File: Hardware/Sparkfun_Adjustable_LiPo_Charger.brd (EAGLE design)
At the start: 31.8 x 31.8 mm, 26 parts, among them SW1 DIP-06, U1 MCP73831

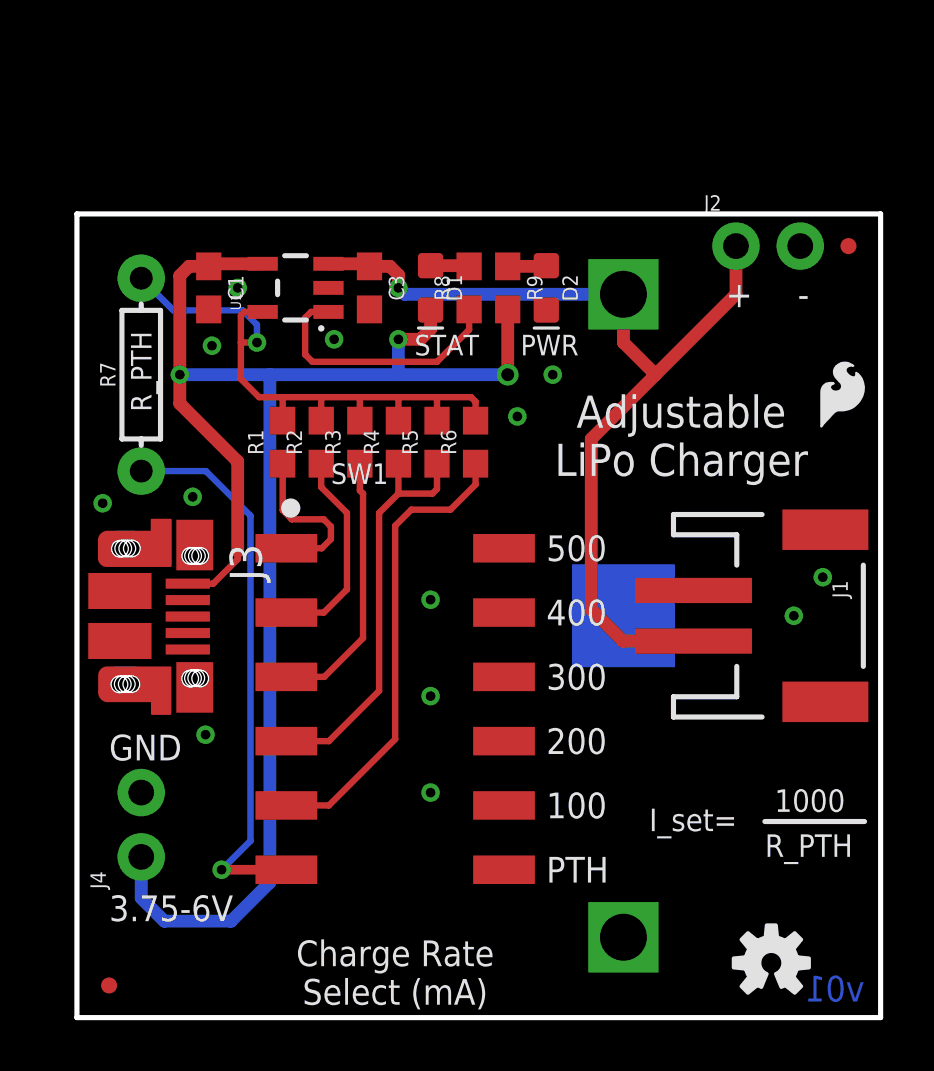
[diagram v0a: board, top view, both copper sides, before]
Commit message: Design Review Changes
Replaced PTH coin cell holder with SMD
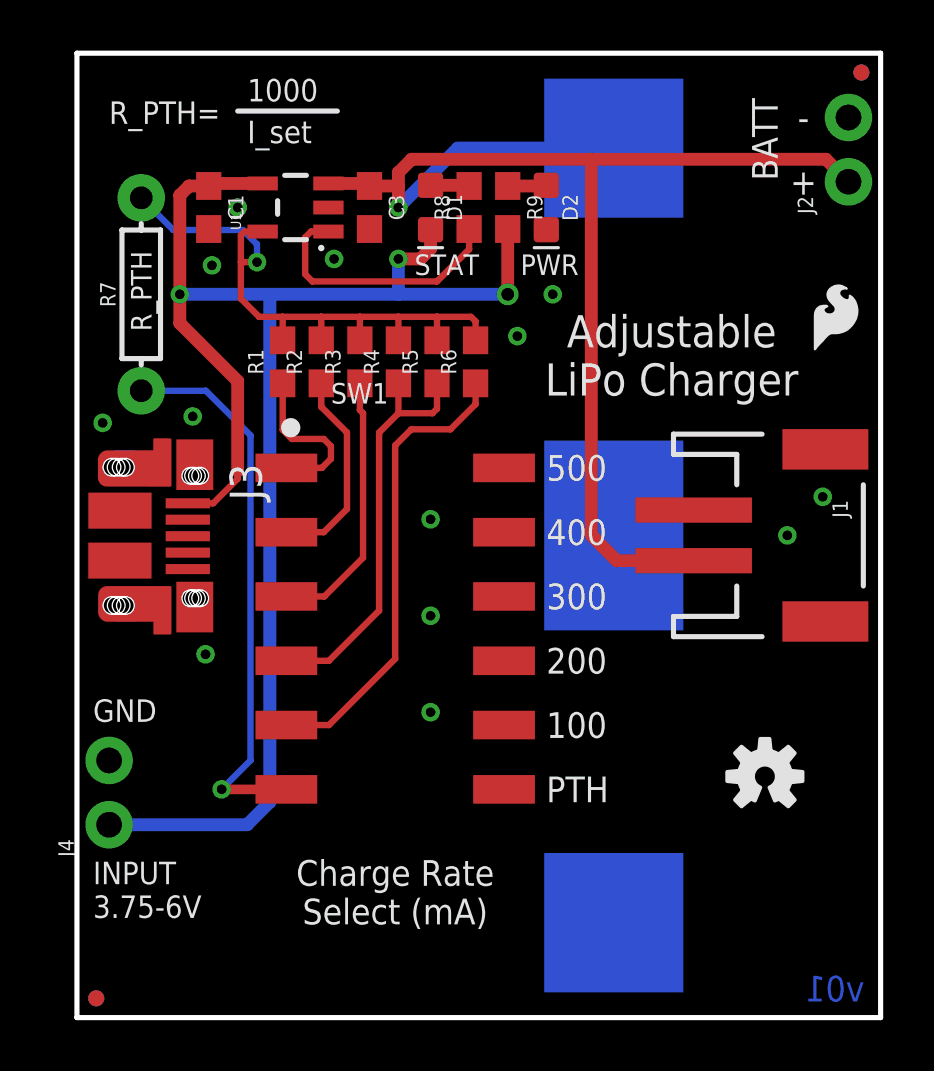
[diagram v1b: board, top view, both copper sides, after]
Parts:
- added FD3, FD4: FIDUCIALUFIDUCIAL, SparkFun-Aesthetics:FIDUCIAL-MICRO
- BT1: device SparkFun-Batteries:BATTCON_24.5MM_PTH -> SparkFun-Batteries:BATTCON_24.5MM_SMD
- moved LOGO2 7.37 mm to (27.2, 9.53)
- moved FD1 6.88 mm to (31.0, 37.3)
- moved J2 5.12 mm to (30.5, 33.0), turned to 90 degrees
- moved U$1 3.29 mm to (15.6, 1.91)
- moved BT1 3.20 mm to (21.2, 19.1)
- moved J1 3.18 mm to (28.1, 19.1)
- moved J3 3.18 mm to (3.05, 19.1)
- moved R1 3.18 mm to (8.13, 25.9)
- moved R2 3.18 mm to (9.65, 25.9)
- moved R3 3.18 mm to (11.2, 25.9)
- moved R4 3.18 mm to (12.7, 25.9)
- moved R5 3.18 mm to (14.2, 25.9)
- moved R6 3.18 mm to (15.7, 25.9)
- moved R7 3.18 mm to (2.54, 28.6)
- moved SW1 3.18 mm to (12.6, 15.4)
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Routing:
- net V_BATT: track 37.5 -> 51.4 mm
- net VCC: track 64.9 -> 63.9 mm
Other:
- board size 31.8 x 31.8 mm -> 31.8 x 38.1 mm
- board text added: "BATT"
- board text added: "INPUT 3.75-6V"
- board text added: "I_set"
- board text added: "R_PTH="
- board text removed: "3.75-6V"
- board text removed: "I_set="

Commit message: Proto Changes
Fixed layout error of D1 to the correct orientation
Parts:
- turned D1 to 90 degrees
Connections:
- net N$8: now also D1.C; no longer D1.A
- net VCC: now also D1.A; no longer D1.C
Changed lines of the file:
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@@
 <setting verticaltext="up"/>
 </settings>
-<grid distance="0.1" unitdist="inch" unit="inch" style="lines" multiple="1" display="yes" altdistance="0.005" altunitdist="inch" altunit="inch"/>
+<grid distance="0.05" unitdist="inch" unit="inch" style="lines" multiple="1" display="yes" altdistance="0.005" altunitdist="inch" altunit="inch"/>
 <layers>
 <layer number="1" name="Top" color="4" fill="1" visible="yes" active="yes"/>
@@
 <layer number="20" name="Dimension" color="15" fill="1" visible="yes" active="yes"/>
 <layer number="21" name="tPlace" color="16" fill="1" visible="yes" active="yes"/>
-<layer number="22" name="bPlace" color="14" fill="1" visible="no" active="yes"/>
+<layer number="22" name="bPlace" color="14" fill="1" visible="yes" active="yes"/>
 <layer number="23" name="tOrigins" color="15" fill="1" visible="yes" active="yes"/>
-<layer number="24" name="bOrigins" color="15" fill="1" visible="no" active="yes"/>
+<layer number="24" name="bOrigins" color="15" fill="1" visible="yes" active="yes"/>
 <layer number="25" name="tNames" color="7" fill="1" visible="no" active="yes"/>
 <layer number="26" name="bNames" color="7" fill="1" visible="no" active="yes"/>
@@
 <layer number="43" name="vRestrict" color="2" fill="10" visible="no" active="yes"/>
 <layer number="44" name="Drills" color="7" fill="1" visible="no" active="yes"/>
-<layer number="45" name="Holes" color="7" fill="1" visible="no" active="yes"/>
+<layer number="45" name="Holes" color="7" fill="1" visible="yes" active="yes"/>
 <layer number="46" name="Milling" color="3" fill="1" visible="no" active="yes"/>
 <layer number="47" name="Measures" color="7" fill="1" visible="no" active="yes"/>
@@
 <text x="6.731" y="36.195" size="0.889" layer="21" font="vector" ratio="15">1000</text>
 <wire x1="6.35" y1="35.814" x2="10.287" y2="35.814" width="0.2032" layer="21"/>
-<text x="28.702" y="33.02" size="1.016" layer="21" font="vector" ratio="15" align="center">+</text>
-<text x="28.702" y="35.56" size="1.016" layer="21" font="vector" ratio="15" align="center">-</text>
+<text x="28.829" y="33.02" size="1.016" layer="21" font="vector" ratio="15" rot="R180" align="center">+</text>
+<text x="28.702" y="35.56" size="1.016" layer="21" font="vector" ratio="15" rot="R90" align="center">-</text>
 <text x="23.495" y="26.162" size="1.27" layer="21" font="vector" ratio="15" align="center">Adjustable
 LiPo Charger</text>
 <text x="2.54" y="28.702" size="0.8128" layer="21" font="vector" ratio="15" rot="R90" align="center">R_PTH</text>
 <text x="28.702" y="33.02" size="1.016" layer="22" font="vector" ratio="15" rot="MR0" align="center">+</text>
-<text x="28.702" y="35.56" size="1.016" layer="22" font="vector" ratio="15" rot="MR0" align="center">-</text>
+<text x="28.702" y="35.56" size="1.016" layer="22" font="vector" ratio="15" rot="MR270" align="center">-</text>
 <text x="0.635" y="3.937" size="0.889" layer="21" font="vector" ratio="15">INPUT
 3.75-6V</text>
@@
 <attribute name="PROD_ID" value="CAP-08280" x="11.557" y="32.004" size="1.778" layer="27" rot="R270" display="off"/>
 </element>
-<element name="D1" library="SparkFun-LED" package="LED-0603" value="BLUE" x="13.97" y="32.004" rot="R270">
-<attribute name="PROD_ID" value="DIO-08575" x="13.97" y="32.004" size="1.778" layer="27" rot="R270" display="off"/>
+<element name="D1" library="SparkFun-LED" package="LED-0603" value="BLUE" x="13.97" y="32.004" rot="SR90">
+<attribute name="PROD_ID" value="DIO-08575" x="13.97" y="32.004" size="1.778" layer="27" rot="SR90" display="off"/>
 </element>
 <element name="FD1" library="SparkFun-Aesthetics" package="FIDUCIAL-MICRO" value="FIDUCIALUFIDUCIAL" x="30.988" y="37.338"/>
@@
 <wire x1="6.858" y1="10.16" x2="5.715" y2="9.017" width="0.254" layer="16"/>
 </signal>
-<signal name="N$8">
-<contactref element="R8" pad="2"/>
-<contactref element="D1" pad="A"/>
-<wire x1="13.97" y1="32.881" x2="15.494" y2="32.881" width="0.508" layer="1"/>
-<wire x1="15.494" y1="32.881" x2="15.494" y2="32.854" width="0.508" layer="1"/>
-</signal>
 <signal name="PROG">
 <contactref element="U1" pad="5"/>
@@
 <contactref element="U1" pad="4"/>
 <contactref element="C1" pad="1"/>
-<contactref element="D1" pad="C"/>
 <via x="12.7" y="29.972" extent="1-16" drill="0.381"/>
 <wire x1="6.35" y1="21.59" x2="6.35" y2="25.146" width="0.508" layer="1"/>
@@
 <wire x1="12.7" y1="29.972" x2="13.56839375" y2="29.972" width="0.508" layer="1"/>
 <wire x1="13.56839375" y1="29.972" x2="13.97" y2="30.37360625" width="0.508" layer="1"/>
-<wire x1="13.97" y1="30.37360625" x2="13.97" y2="31.127" width="0.508" layer="1"/>
 <wire x1="7.3359" y1="32.954" x2="5.207" y2="32.954" width="0.508" layer="1"/>
 <wire x1="5.207" y1="32.954" x2="5.207" y2="32.854" width="0.508" layer="1"/>
@@
 <wire x1="6.72571875" y1="7.62" x2="1.27" y2="7.62" width="0.508" layer="16"/>
 <wire x1="7.62" y1="8.51428125" x2="6.72571875" y2="7.62" width="0.508" layer="16"/>
+<contactref element="D1" pad="A"/>
+<wire x1="13.97" y1="30.37360625" x2="13.97" y2="31.127" width="0.508" layer="1"/>
 </signal>
 <signal name="N$1">
@@
 <wire x1="18.542" y1="32.854" x2="18.542" y2="32.881" width="0.508" layer="1"/>
 </signal>
+<signal name="N$8">
+<contactref element="R8" pad="2"/>
+<contactref element="D1" pad="C"/>
+<wire x1="13.97" y1="32.881" x2="15.467" y2="32.881" width="0.254" layer="1"/>
+<wire x1="15.467" y1="32.881" x2="15.494" y2="32.854" width="0.254" layer="1"/>
+</signal>
 </signals>

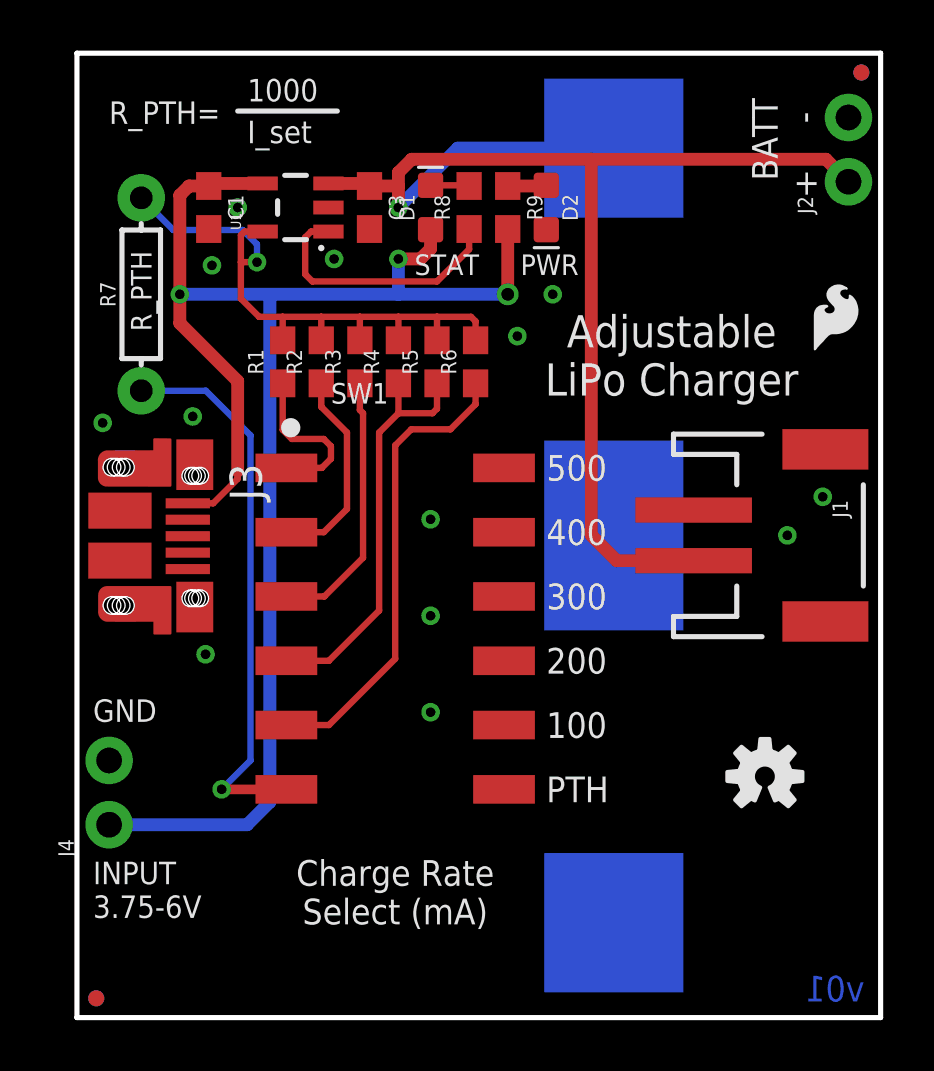
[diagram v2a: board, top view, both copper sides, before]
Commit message: v10 changes
- Added switch label to indicate on/off position.
- Added units to charge rate equation
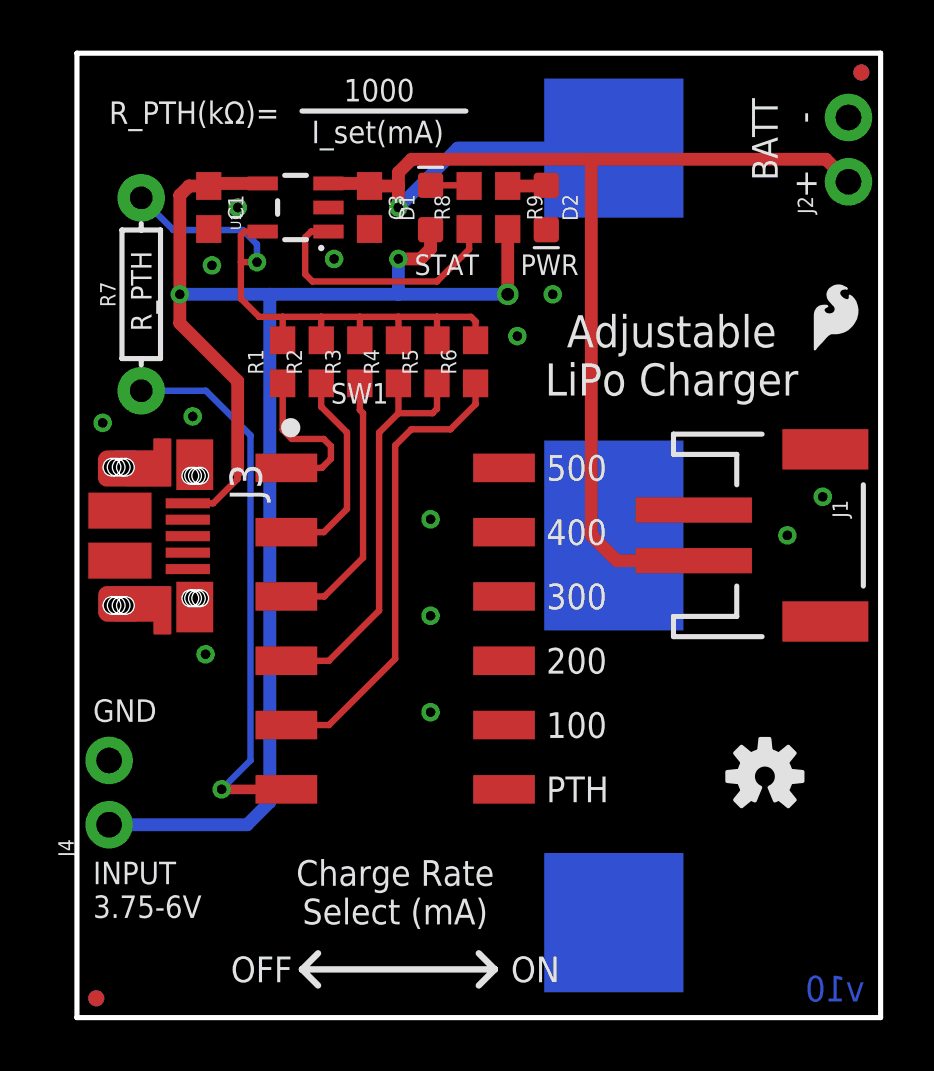
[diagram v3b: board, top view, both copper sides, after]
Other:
- board text added: "I_set(mA)"
- board text added: "OFF"
- board text added: "ON"
- board text added: "R_PTH(kΩ)="
- board text added: "v10"
- board text removed: "I_set"
- board text removed: "R_PTH="
- board text removed: "v01"
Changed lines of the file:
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@@
 <layer number="20" name="Dimension" color="15" fill="1" visible="yes" active="yes"/>
 <layer number="21" name="tPlace" color="16" fill="1" visible="yes" active="yes"/>
-<layer number="22" name="bPlace" color="14" fill="1" visible="yes" active="yes"/>
+<layer number="22" name="bPlace" color="14" fill="1" visible="no" active="yes"/>
 <layer number="23" name="tOrigins" color="15" fill="1" visible="yes" active="yes"/>
 <layer number="24" name="bOrigins" color="15" fill="1" visible="yes" active="yes"/>
@@
 <layer number="37" name="tTest" color="7" fill="1" visible="no" active="yes"/>
 <layer number="38" name="bTest" color="7" fill="1" visible="no" active="yes"/>
-<layer number="39" name="tKeepout" color="4" fill="11" visible="no" active="yes"/>
-<layer number="40" name="bKeepout" color="1" fill="11" visible="no" active="yes"/>
+<layer number="39" name="tKeepout" color="4" fill="11" visible="yes" active="yes"/>
+<layer number="40" name="bKeepout" color="1" fill="11" visible="yes" active="yes"/>
 <layer number="41" name="tRestrict" color="4" fill="10" visible="no" active="yes"/>
 <layer number="42" name="bRestrict" color="1" fill="10" visible="no" active="yes"/>
 <layer number="43" name="vRestrict" color="2" fill="10" visible="no" active="yes"/>
 <layer number="44" name="Drills" color="7" fill="1" visible="no" active="yes"/>
-<layer number="45" name="Holes" color="7" fill="1" visible="yes" active="yes"/>
+<layer number="45" name="Holes" color="7" fill="1" visible="no" active="yes"/>
 <layer number="46" name="Milling" color="3" fill="1" visible="no" active="yes"/>
-<layer number="47" name="Measures" color="7" fill="1" visible="no" active="yes"/>
+<layer number="47" name="Measures" color="7" fill="1" visible="yes" active="yes"/>
 <layer number="48" name="Document" color="7" fill="1" visible="no" active="yes"/>
 <layer number="49" name="Reference" color="7" fill="1" visible="no" active="yes"/>
@@
 Select (mA)</text>
 <text x="17.78" y="-20.32" size="1.778" layer="51" font="vector" ratio="15">Alex Wende</text>
-<text x="6.731" y="34.544" size="0.889" layer="21" font="vector" ratio="15">I_set</text>
-<text x="1.27" y="35.306" size="0.889" layer="21" font="vector" ratio="15">R_PTH=</text>
-<text x="6.731" y="36.195" size="0.889" layer="21" font="vector" ratio="15">1000</text>
-<wire x1="6.35" y1="35.814" x2="10.287" y2="35.814" width="0.2032" layer="21"/>
+<text x="9.271" y="34.544" size="0.889" layer="21" font="vector" ratio="15">I_set(mA)</text>
+<text x="1.27" y="35.306" size="0.889" layer="21" font="vector" ratio="15">R_PTH(kΩ)=</text>
+<text x="10.541" y="36.195" size="0.889" layer="21" font="vector" ratio="15">1000</text>
+<wire x1="8.89" y1="35.814" x2="15.367" y2="35.814" width="0.2032" layer="21"/>
 <text x="28.829" y="33.02" size="1.016" layer="21" font="vector" ratio="15" rot="R180" align="center">+</text>
 <text x="28.702" y="35.56" size="1.016" layer="21" font="vector" ratio="15" rot="R90" align="center">-</text>
@@
 <text x="3.302" y="7.112" size="1.016" layer="22" font="vector" ratio="15" rot="MR0">+</text>
 <text x="3.302" y="9.652" size="1.016" layer="22" font="vector" ratio="15" rot="MR0">-</text>
-<text x="31.115" y="0.635" size="1.016" layer="16" font="vector" ratio="20" rot="MR0">v01</text>
+<text x="31.115" y="0.635" size="1.016" layer="16" font="vector" ratio="20" rot="MR0">v10</text>
 <dimension x1="0" y1="0" x2="0" y2="38.1" x3="-5.08" y3="19.05" textsize="1.016" textratio="15" layer="47" unit="inch"/>
 <dimension x1="0" y1="0" x2="31.75" y2="0" x3="15.875" y3="-5.08" textsize="1.016" textratio="15" layer="47" unit="inch"/>
@@
 <text x="17.526" y="29.337" size="0.8128" layer="21" font="vector" ratio="15">PWR</text>
 <text x="26.67" y="36.322" size="1.016" layer="21" font="vector" ratio="15" rot="R270">BATT</text>
+<text x="8.509" y="1.905" size="1.016" layer="21" font="vector" ratio="15" rot="R180" align="center-left">OFF</text>
+<text x="17.145" y="1.905" size="1.016" layer="21" font="vector" ratio="15" align="center-left">ON</text>
+<wire x1="8.89" y1="1.905" x2="16.51" y2="1.905" width="0.254" layer="21"/>
+<wire x1="16.51" y1="1.905" x2="15.875" y2="2.54" width="0.254" layer="21"/>
+<wire x1="16.51" y1="1.905" x2="15.875" y2="1.27" width="0.254" layer="21"/>
+<wire x1="8.89" y1="1.905" x2="9.525" y2="1.27" width="0.254" layer="21"/>
+<wire x1="8.89" y1="1.905" x2="9.525" y2="2.54" width="0.254" layer="21"/>
 </plain>
 <attributes>
